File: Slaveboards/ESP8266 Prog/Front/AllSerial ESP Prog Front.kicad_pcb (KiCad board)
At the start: 2 copper layers, 71.5 x 24 mm, 5 parts

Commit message: Improve libraries
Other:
- board text added: "JLCJLCJLCJLC"
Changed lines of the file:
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@@
 		(fp_arc
 			(start -32.748941 -24.000005)
-			(mid -32.664859 -23.981455)
+			(mid -32.66486 -23.981455)
 			(end -32.596368 -23.929275)
 			(stroke
@@
 		(fp_arc
 			(start -29.285718 -13.690937)
-			(mid -29.259139 -13.636637)
+			(mid -29.259139 -13.636636)
 			(end -29.25 -13.576875)
 			(stroke
@@
 		(fp_arc
 			(start -29.129359 -0.680846)
-			(mid -29.094247 -0.709679)
+			(mid -29.094246 -0.709679)
 			(end -29.05 -0.719996)
 			(stroke
@@
 		(fp_arc
 			(start 29.05 -0.719996)
-			(mid 29.094244 -0.709675)
+			(mid 29.094246 -0.709678)
 			(end 29.129359 -0.680846)
 			(stroke
@@
 		(fp_arc
 			(start 29.129359 -23.319156)
-			(mid 29.094247 -23.290322)
+			(mid 29.094247 -23.290323)
 			(end 29.050001 -23.280005)
 			(stroke
@@
 		(fp_arc
 			(start 29.249999 -13.616875)
-			(mid 29.259133 -13.676636)
+			(mid 29.259134 -13.676636)
 			(end 29.285709 -13.730937)
 			(stroke
@@
 		(fp_arc
 			(start 29.25 -10.819996)
-			(mid 29.308577 -10.96142)
+			(mid 29.308579 -10.961417)
 			(end 29.45 -11.019996)
 			(stroke
@@
 		(fp_arc
 			(start 29.285708 -13.730937)
-			(mid 30.208301 -14.593559)
+			(mid 30.208298 -14.593561)
 			(end 31.404168 -14.999996)
 			(stroke
@@
 		(fp_arc
 			(start 29.285709 -10.309065)
-			(mid 29.259126 -10.363365)
+			(mid 29.259135 -10.363365)
 			(end 29.25 -10.423125)
 			(stroke
@@
 		(fp_arc
 			(start 29.45 -13.019996)
-			(mid 29.308577 -13.078574)
+			(mid 29.308579 -13.078575)
 			(end 29.25 -13.219996)
 			(stroke
@@
 		(fp_arc
 			(start 29.591266 -23.921688)
-			(mid 29.745026 -23.999949)
+			(mid 29.745024 -23.999944)
 			(end 29.902481 -23.929425)
 			(stroke
@@
 		(fp_arc
 			(start 29.902479 -0.070575)
-			(mid 29.745025 -0.00006)
+			(mid 29.745023 -0.000058)
 			(end 29.591268 -0.078315)
 			(stroke
@@
 		(fp_arc
 			(start 30.098618 -13.019996)
-			(mid 30.180278 -13.002576)
+			(mid 30.180273 -13.002575)
 			(end 30.247701 -12.953336)
 			(stroke
@@
 		(fp_arc
 			(start 30.247698 -11.086664)
-			(mid 30.535038 -11.21979)
+			(mid 30.53505 -11.219856)
 			(end 30.829168 -11.102356)
 			(stroke
@@
 		(fp_arc
 			(start 30.2477 -11.086665)
-			(mid 30.180276 -11.037423)
+			(mid 30.180274 -11.037422)
 			(end 30.098619 -11.019995)
 			(stroke
@@
 		(fp_arc
 			(start 30.423759 -0.684715)
-			(mid 30.5 -0.720004)
+			(mid 30.5 -0.720003)
 			(end 30.57624 -0.684714)
 			(stroke
@@
 		(fp_arc
 			(start 30.829167 -12.937646)
-			(mid 30.535037 -12.82009)
+			(mid 30.535051 -12.820146)
 			(end 30.2477 -12.953337)
 			(stroke
@@
 		(fp_arc
 			(start 30.829168 -12.937646)
-			(mid 30.991003 -13.075431)
+			(mid 30.991003 -13.07543)
 			(end 31.173131 -13.184996)
 			(stroke
@@
 		(fp_arc
 			(start 31.097515 -23.929424)
-			(mid 31.259507 -23.99978)
+			(mid 31.259505 -23.999775)
 			(end 31.414081 -23.914356)
 			(stroke
@@
 		(fp_arc
 			(start 31.173131 -13.184996)
-			(mid 31.749999 -13.620001)
+			(mid 31.749995 -13.62001)
 			(end 32.326859 -13.184995)
 			(stroke
@@
 		(fp_arc
 			(start 31.173131 -10.854996)
-			(mid 30.991007 -10.964572)
+			(mid 30.991003 -10.964567)
 			(end 30.829168 -11.102356)
 			(stroke
@@
 		(fp_arc
 			(start 31.923759 -0.684715)
-			(mid 31.999993 -0.720004)
+			(mid 31.999993 -0.720002)
 			(end 32.076231 -0.684724)
 			(stroke
@@
 		(fp_arc
 			(start 32.079068 -23.315365)
-			(mid 32.001494 -23.278334)
+			(mid 32.001488 -23.278337)
 			(end 31.923831 -23.315204)
 			(stroke
@@
 		(fp_arc
 			(start 32.095831 -14.999996)
-			(mid 32.231689 -14.981077)
+			(mid 32.231689 -14.981076)
 			(end 32.36654 -14.955965)
 			(stroke
@@
 		(fp_arc
 			(start 32.25 -21.980006)
-			(mid 32.603556 -21.83356)
+			(mid 32.603553 -21.833559)
 			(end 32.75 -21.480006)
 			(stroke
@@
 		(fp_arc
 			(start 32.326859 -13.184996)
-			(mid 32.669228 -12.93923)
+			(mid 32.66923 -12.939231)
 			(end 32.915 -12.596864)
 			(stroke
@@
 		(fp_arc
 			(start 32.326859 -10.854996)
-			(mid 31.749999 -10.420006)
+			(mid 31.749995 -10.419982)
 			(end 31.173131 -10.854995)
 			(stroke
@@
 		(fp_arc
 			(start 32.366539 -14.955965)
-			(mid 32.442788 -14.922176)
+			(mid 32.442794 -14.922183)
 			(end 32.49864 -14.860237)
 			(stroke
@@
 		(fp_arc
 			(start 32.386358 -9.088265)
-			(mid 30.650958 -9.228609)
+			(mid 30.650958 -9.228601)
 			(end 29.285709 -10.309065)
 			(stroke
@@
 		(fp_arc
 			(start 32.386359 -9.088265)
-			(mid 32.638289 -9.028644)
+			(mid 32.638293 -9.028647)
 			(end 32.749999 -8.795094)
 			(stroke
@@
 		(fp_arc
 			(start 32.599138 -23.929276)
-			(mid 32.66736 -23.981322)
+			(mid 32.667357 -23.981325)
 			(end 32.751109 -23.999996)
 			(stroke
@@
 		(fp_arc
 			(start 32.74894 0.000002)
-			(mid 32.664858 -0.018548)
+			(mid 32.66486 -0.018547)
 			(end 32.596368 -0.070725)
 			(stroke
@@
 		(fp_arc
 			(start 32.75 -5.219996)
-			(mid 32.808577 -5.36142)
+			(mid 32.808579 -5.361417)
 			(end 32.95 -5.419996)
 			(stroke
@@
 		(fp_arc
 			(start 32.75 -2.519996)
-			(mid 32.603552 -2.166445)
+			(mid 32.603553 -2.166443)
 			(end 32.25 -2.019996)
 			(stroke
@@
 		(fp_arc
 			(start 32.751879 -23.999996)
-			(mid 34.873535 -23.1215)
+			(mid 34.873527 -23.121497)
 			(end 35.752381 -20.999996)
 			(stroke
@@
 		(fp_arc
 			(start 32.75294 -16.579996)
-			(mid 32.811514 -16.721441)
+			(mid 32.811519 -16.721417)
 			(end 32.95294 -16.779996)
 			(stroke
@@
 		(fp_arc
 			(start 32.77974 -14.773365)
-			(mid 32.759741 -14.821597)
+			(mid 32.759757 -14.821601)
 			(end 32.75294 -14.873365)
 			(stroke
@@
 		(fp_arc
 			(start 32.915 -12.596865)
-			(mid 33.349999 -12.02)
+			(mid 33.350014 -12.020001)
 			(end 32.914999 -11.443137)
 			(stroke
@@
 		(fp_arc
 			(start 32.915 -11.443137)
-			(mid 32.669231 -11.100766)
+			(mid 32.669231 -11.100765)
 			(end 32.32686 -10.854995)
 			(stroke
@@
 		(fp_arc
 			(start 32.95 -18.580006)
-			(mid 32.808581 -18.638585)
+			(mid 32.808579 -18.638585)
 			(end 32.75 -18.780006)
 			(stroke
@@
 		(fp_arc
 			(start 32.95 -7.219996)
-			(mid 32.808577 -7.278574)
+			(mid 32.808579 -7.278575)
 			(end 32.75 -7.419996)
 			(stroke
@@
 		(fp_arc
 			(start 33.574159 -13.197375)
-			(mid 33.498292 -13.187426)
+			(mid 33.498279 -13.187384)
 			(end 33.437559 -13.233975)
 			(stroke
@@
 		(fp_arc
 			(start 33.74648 -13.498915)
-			(mid 33.594718 -13.478958)
+			(mid 33.594712 -13.478936)
 			(end 33.473268 -13.572125)
 			(stroke
@@
 		(fp_arc
 			(start 33.89019 -14.849996)
-			(mid 33.890188 -14.95)
+			(mid 33.890189 -14.949995)
 			(end 33.97679 -14.999995)
 			(stroke
@@
 		(fp_arc
 			(start 33.976789 -14.699996)
-			(mid 33.976789 -14.900003)
+			(mid 33.976792 -14.899997)
 			(end 34.15 -14.999996)
 			(stroke
@@
 		(fp_arc
 			(start 34.3393 -14.072125)
-			(mid 34.359308 -13.920351)
+			(mid 34.359279 -13.920358)
 			(end 34.26609 -13.798915)
 			(stroke
@@
 		(fp_arc
 			(start 34.47679 -13.833975)
-			(mid 34.486754 -13.758102)
+			(mid 34.486781 -13.758095)
 			(end 34.44019 -13.697375)
 			(stroke
@@
 		(fp_arc
 			(start 34.947158 -14.999996)
-			(mid 35.023696 -14.98478)
+			(mid 35.023695 -14.984776)
 			(end 35.088581 -14.941425)
 			(stroke
@@
 		(fp_arc
 			(start 35.06539 -12.013765)
-			(mid 35.030104 -12.09)
+			(mid 35.030107 -12.090001)
 			(end 35.065389 -12.166237)
 			(stroke
@@
 		(fp_arc
 			(start 35.06539 -9.013765)
-			(mid 35.030104 -9.09)
+			(mid 35.030107 -9.090001)
 			(end 35.065389 -9.166237)
 			(stroke
@@
 		(fp_arc
 			(start 35.06539 -7.513765)
-			(mid 35.030104 -7.59)
+			(mid 35.030107 -7.590001)
 			(end 35.065389 -7.666237)
 			(stroke
@@
 		(fp_arc
 			(start 35.07169 -16.320956)
-			(mid 35.033027 -16.395538)
+			(mid 35.033046 -16.395537)
 			(end 35.064891 -16.473264)
 			(stroke
@@
 		(fp_arc
 			(start 35.088617 -15.046515)
-			(mid 35.028587 -15.012008)
+			(mid 35.028592 -15.011985)
 			(end 34.96039 -14.999996)
 			(stroke
@@
 		(fp_arc
 			(start 35.675449 -15.853087)
-			(mid 35.752911 -15.699568)
+			(mid 35.752891 -15.699569)
 			(end 35.68254 -15.542675)
 			(stroke
@@
 		(fp_arc
 			(start 35.679439 -8.492466)
-			(mid 35.750001 -8.340001)
+			(mid 35.750001 -8.340002)
 			(end 35.67944 -8.187537)
 			(stroke
@@
 		(fp_arc
 			(start 35.67944 -6.992465)
-			(mid 35.733832 -6.91878)
+			(mid 35.733831 -6.91878)
 			(end 35.749668 -6.828575)
 			(stroke
@@
 		(fp_arc
 			(start 35.691417 -14.338575)
-			(mid 35.734799 -14.2737)
+			(mid 35.734773 -14.273692)
 			(end 35.75 -14.197156)
 			(stroke
@@
 		(fp_arc
 			(start 35.749439 -2.999996)
-			(mid 34.870587 -0.878496)
+			(mid 34.870586 -0.878496)
 			(end 32.74894 0.000003)
 			(stroke
@@
 		(fp_arc
 			(start 35.749999 -12.839996)
-			(mid 35.731503 -12.755999)
+			(mid 35.731504 -12.755998)
 			(end 35.67944 -12.687537)
 			(stroke
@@
 		(fp_arc
 			(start 35.749999 -9.839996)
-			(mid 35.731503 -9.755999)
+			(mid 35.731504 -9.755998)
 			(end 35.67944 -9.687537)
 			(stroke
@@
 		(fp_arc
 			(start 35.752381 -17.214526)
-			(mid 35.73913 -17.126549)
+			(mid 35.739137 -17.126547)
 			(end 35.68905 -17.053015)
 			(stroke
@@
 		)
 		(fp_line
-			(start -32.75 -24)
+			(start -32.75 0)
+			(end 32.75 0)
+			(stroke
+				(width 0.05)
+				(type default)
+			)
+			(layer "Edge.Cuts")
+		)
+		(fp_line
+			(start -32.749999 -24)
 			(end 32.75 -24)
-			(stroke
-				(width 0.05)
-				(type solid)
-			)
-			(layer "Edge.Cuts")
-		)
-		(fp_line
-			(start 32.75 0)
-			(end -32.75 0)
 			(stroke
 				(width 0.05)
@@
 			)
 			(justify left bottom mirror)
+		)
+	)
+	(gr_text "JLCJLCJLCJLC"
+		(at 153.0011 114.8036 0)
+		(layer "B.SilkS")
+		(effects
+			(font
+				(size 1 1)
+				(thickness 0.1)
+			)
+			(justify left bottom mirror)

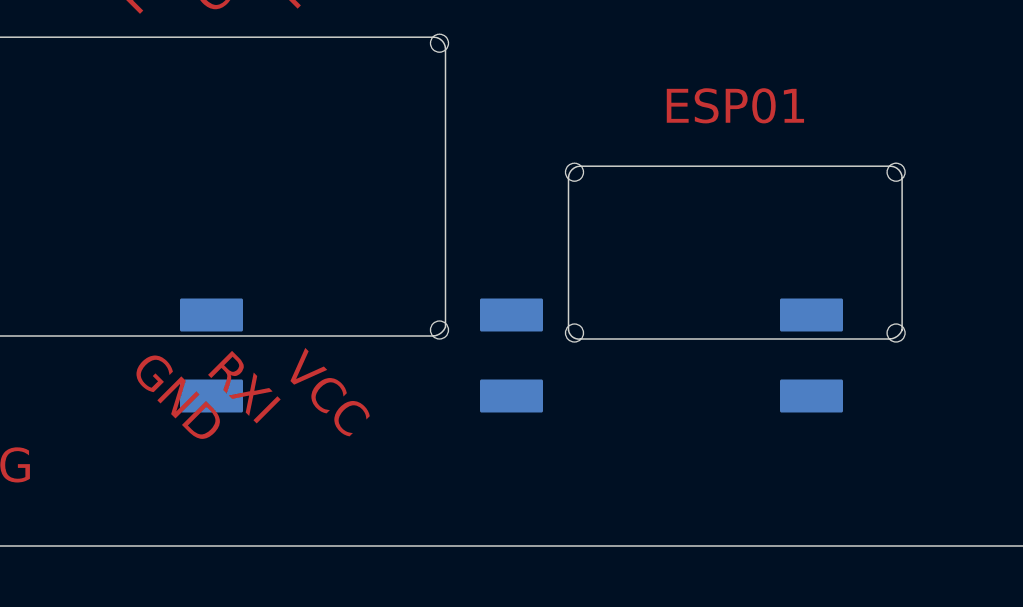
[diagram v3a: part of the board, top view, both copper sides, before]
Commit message: Remove pads from cutouts
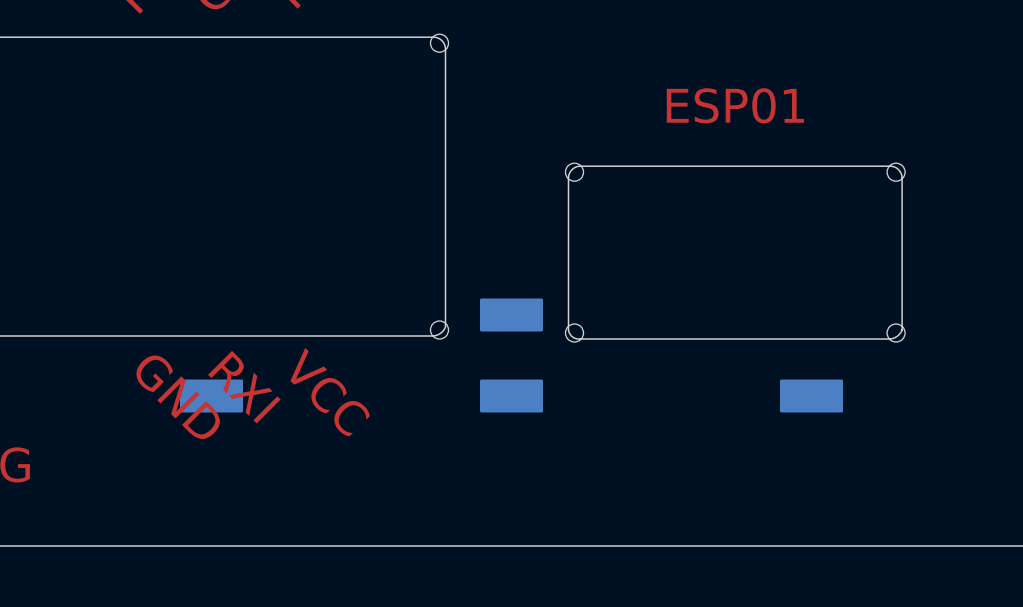
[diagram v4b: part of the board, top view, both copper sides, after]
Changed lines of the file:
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@@
-		)
-		(fp_rect
-			(start -21 -8.2)
-			(end -19 -7.2)
-			(stroke
-				(width 0.1)
-				(type solid)
-			)
-			(fill yes)
-			(layer "B.Cu")
 		)
 		(fp_rect
@@
 			(start -11 -5.5)
 			(end -9 -4.5)
-			(stroke
-				(width 0.1)
-				(type solid)
-			)
-			(fill yes)
-			(layer "B.Cu")
-		)
-		(fp_rect
-			(start -1 -8.2)
-			(end 1 -7.2)
 			(stroke
 				(width 0.1)
@@
 		)
 		(fp_rect
-			(start -21 -8.2)
+			(start -21 -5.5)
 			(end -19 -4.5)
 			(stroke
@@
 		)
 		(fp_rect
-			(start -1 -8.2)
+			(start -1 -5.5)
 			(end 1 -4.5)
 			(stroke

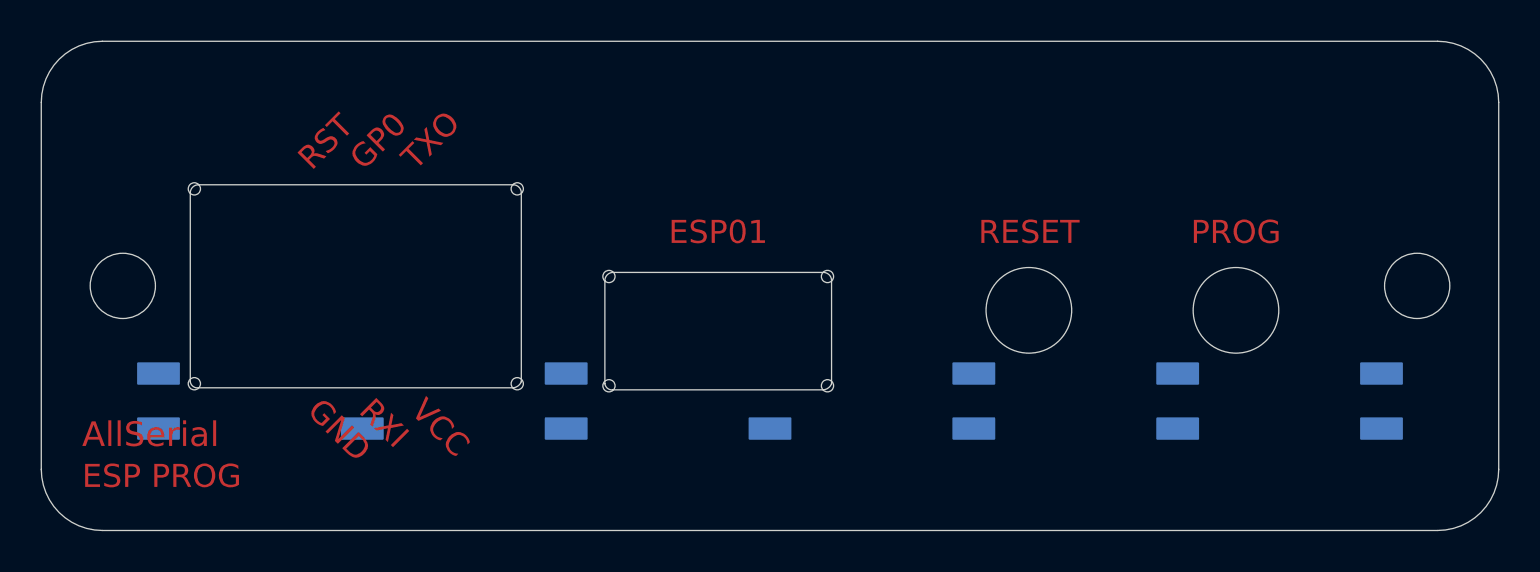
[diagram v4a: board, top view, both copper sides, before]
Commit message: Add python testskript
Add mainboard tester
Add libraries
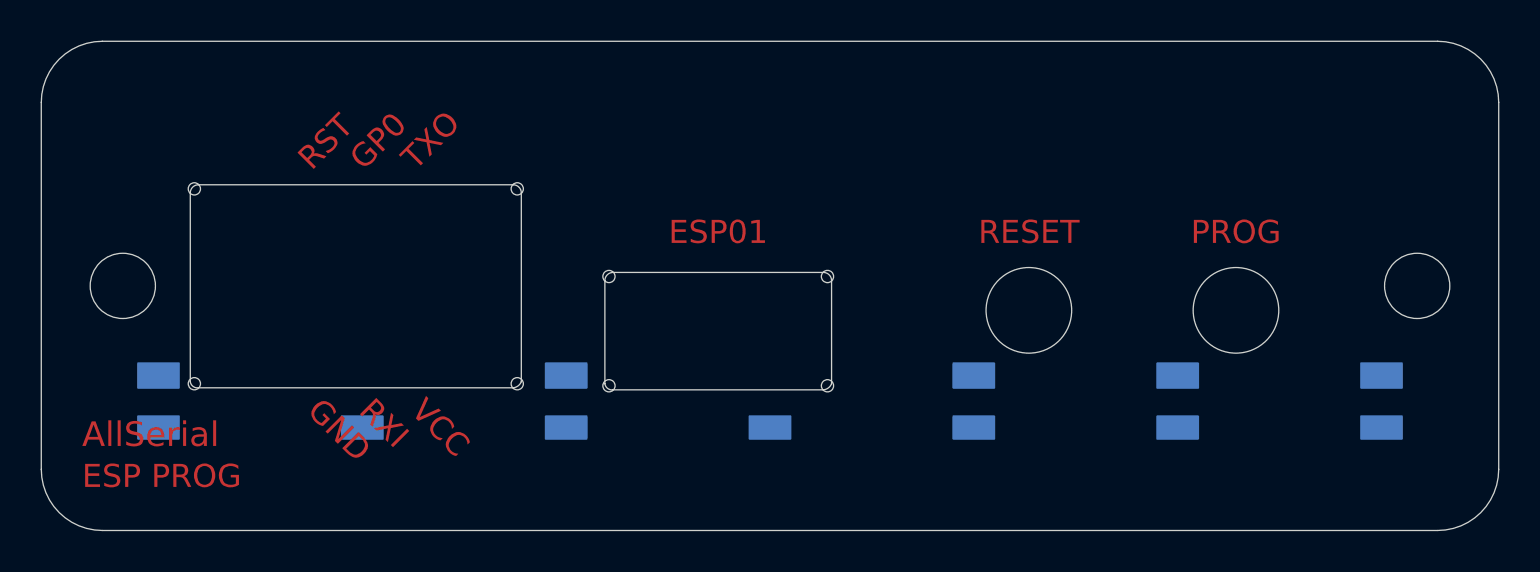
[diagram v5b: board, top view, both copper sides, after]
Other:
- board text added: "AllSerial ESP Prog v2.1 26/25"
- board text removed: "AllSerial ESP Prog Front v2.1 26/25"
- board text removed: "JLCJLCJLCJLC"
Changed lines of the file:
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@@
 		(fp_rect
 			(start -31 -8.2)
-			(end -29 -7.2)
+			(end -29 -7)
 			(stroke
 				(width 0.1)
@@
 		)
 		(fp_rect
-			(start -31 -5.5)
+			(start -31 -5.6)
 			(end -29 -4.5)
 			(stroke
@@
 		)
 		(fp_rect
-			(start -21 -5.5)
+			(start -21 -5.6)
 			(end -19 -4.5)
 			(stroke
@@
 		(fp_rect
 			(start -11 -8.2)
-			(end -9 -7.2)
+			(end -9 -7)
 			(stroke
 				(width 0.1)
@@
 		)
 		(fp_rect
-			(start -11 -5.5)
+			(start -11 -5.6)
 			(end -9 -4.5)
 			(stroke
@@
 		)
 		(fp_rect
-			(start -1 -5.5)
+			(start -1 -5.6)
 			(end 1 -4.5)
 			(stroke
@@
 		(fp_rect
 			(start 9 -8.2)
-			(end 11 -7.2)
+			(end 11 -7)
 			(stroke
 				(width 0.1)
@@
 		)
 		(fp_rect
-			(start 9 -5.5)
+			(start 9 -5.6)
 			(end 11 -4.5)
 			(stroke
@@
 		(fp_rect
 			(start 19 -8.2)
-			(end 21 -7.2)
+			(end 21 -7)
 			(stroke
 				(width 0.1)
@@
 		)
 		(fp_rect
-			(start 19 -5.5)
+			(start 19 -5.6)
 			(end 21 -4.5)
 			(stroke
@@
 		(fp_rect
 			(start 29 -8.2)
-			(end 31 -7.2)
+			(end 31 -7)
 			(stroke
 				(width 0.1)
@@
 		)
 		(fp_rect
-			(start 29 -5.5)
+			(start 29 -5.6)
 			(end 31 -4.5)
 			(stroke
@@
 		)
 		(fp_rect
-			(start -21 -5.5)
+			(start -21 -8.2)
 			(end -19 -4.5)
 			(stroke
@@
 		)
 		(fp_rect
-			(start -1 -5.5)
+			(start -1 -8.2)
 			(end 1 -4.5)
 			(stroke
@@
 		)
 	)
-	(gr_text "AllSerial ESP Prog Front v2.1 26/25"
-		(at 173.9011 97.9536 0)
+	(gr_text "AllSerial ESP Prog v2.1 26/25"
+		(at 148.5011 98.3346 0)
 		(layer "B.SilkS")
 		(effects
@@
 				(thickness 0.14224)
 			)
-			(justify left bottom mirror)
-		)
-	)
-	(gr_text "JLCJLCJLCJLC"
-		(at 153.0011 114.8036 0)
-		(layer "B.SilkS")
-		(effects
-			(font
-				(size 1 1)
-				(thickness 0.1)
-			)
-			(justify left bottom mirror)
-		)
-	)
+			(justify bottom mirror)
+		)
+	)
